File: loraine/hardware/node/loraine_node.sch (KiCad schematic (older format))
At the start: 41 parts, among them CON1 BARREL_JACK, IC1 ATTINY2313A-S, P1 POWER_THRU, P2 POWER, P3 SOLDER_PAD, P4 ICSP, P5 OUTPUTS, P6 BUS, P7 BUS_THRU, Q1 BD679, Q2 BD679, Q3 BD679, Q4 BD679, Q5 BD679, Q6 BD679, Q7 BD679, Q8 BD679, U1 UA7805CKCT, U2 SN65176BD, U3 TL4242, U4 TL4242, U5 TL4242, X1 16MHz

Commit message: Split boards
Removed LEDs and TL4242s and sense resistors from main node board and added 3x SIL3 connectors
Added 2nd board containing heatsunk LED mounting, TL4242, sense resistors.
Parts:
- removed D1: STAR_LED, symbol STAR_LED
- removed R1, R2, R3: R, symbol R
- removed U3, U4, U5: TL4242, symbol TL4242
- added K1, K2, K3: CONN_3, symbol CONN_3
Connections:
- net labels added: +5V
- wire segments 238 -> 154
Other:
- note removed: "3W star wants I=0.35A R=0.51\n1W star wants I=0.15A R=1.18"
- note removed: "Resistor dissipation is\n1W star: 60mW\n3W star: 27mW"
- note removed: "These current sense resistors\nset the peak LED current.\nREF is held at 177mV nominal\n"

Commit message: Proposed output driver for node h/w
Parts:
- removed Q1, Q2, Q3, Q4, Q5, Q6, Q7, Q8: BD679, symbol BD679
- added D?: DIODE, symbol DIODE
- added Q?: PNP, symbol PNP
- added Q?: MOS_N, symbol MOS_N
- added R? (x2): 10k, symbol R
- added R?: 560, symbol R
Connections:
- wire segments 154 -> 141
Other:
- note added: "ATtiny\nOutput"
- note added: "Load"

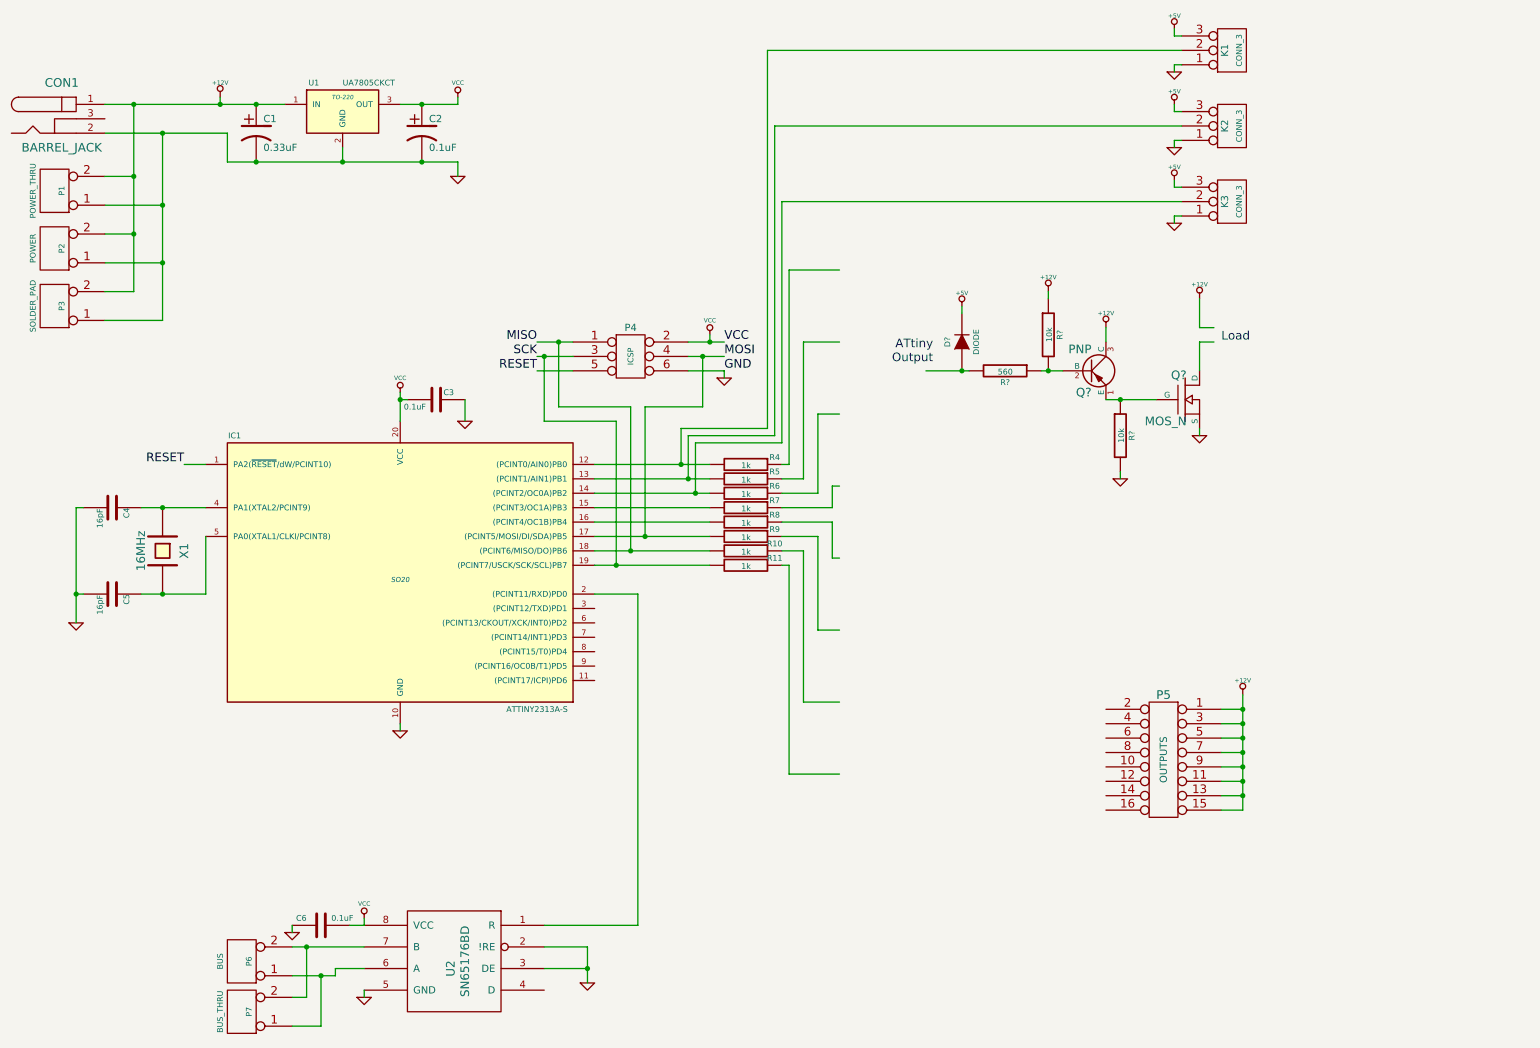
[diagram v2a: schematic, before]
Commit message: NMOS drivers on schematic + ERC fixes
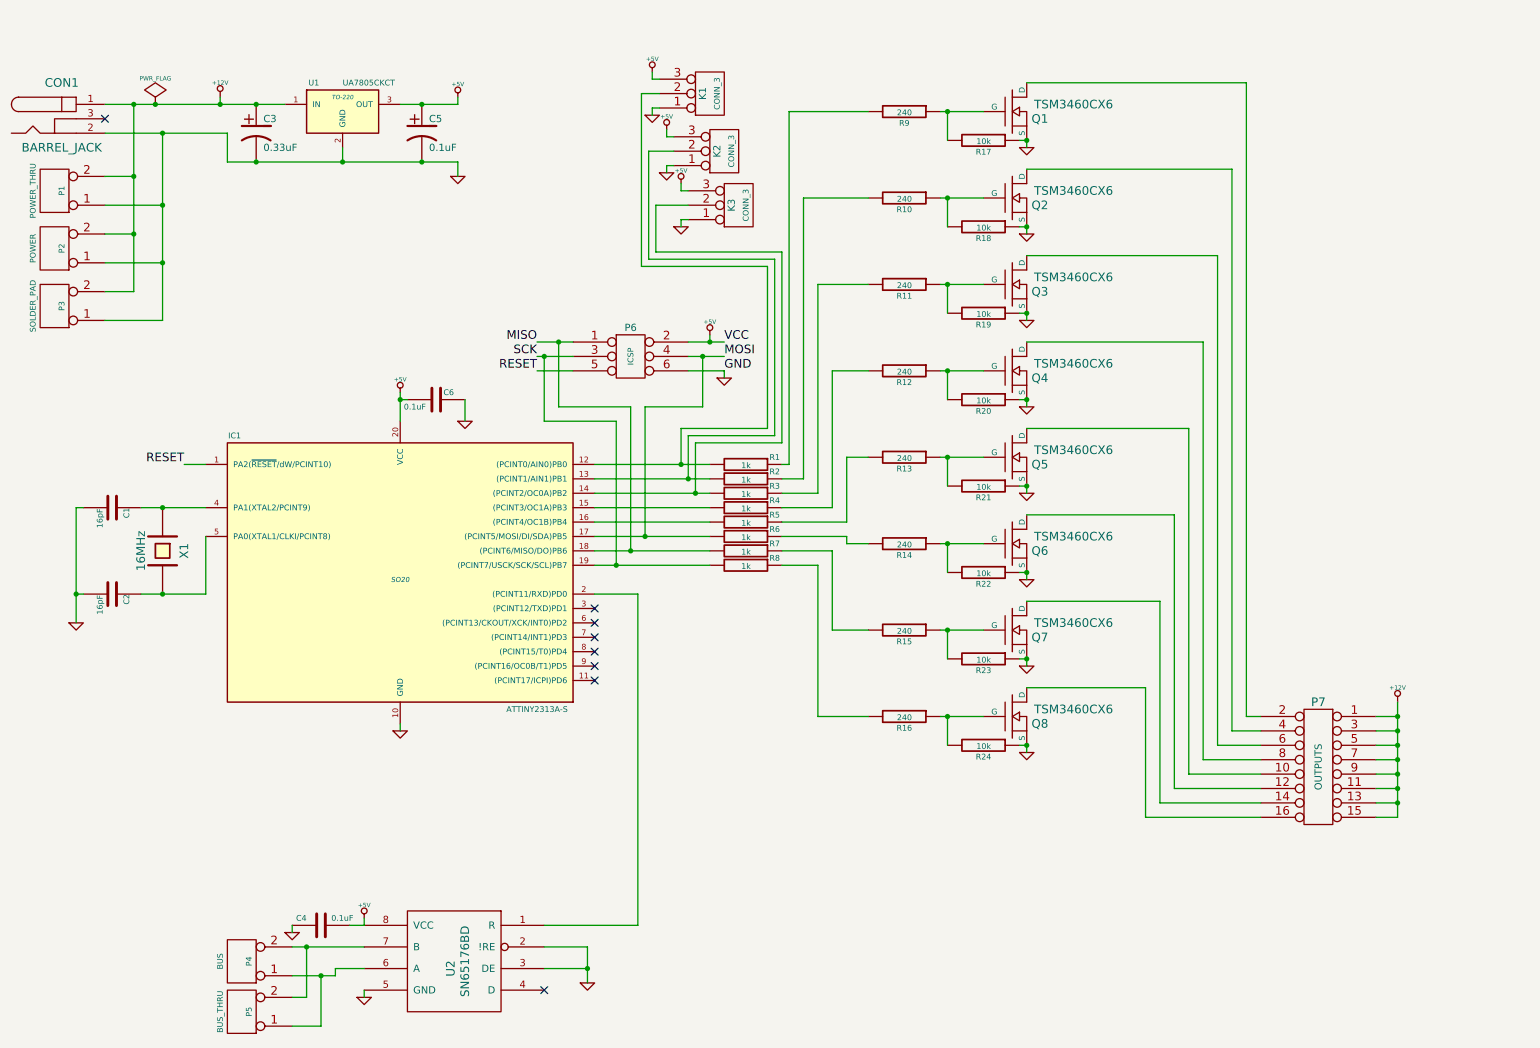
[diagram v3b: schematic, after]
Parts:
- removed D?: DIODE, symbol DIODE
- removed Q?: PNP, symbol PNP
- removed R?: 10k, symbol R
- added Q2, Q3, Q4, Q5, Q6, Q7, Q8: TSM3460CX6, symbol MOS_N
- added R10, R11, R12, R13, R14, R15, R16: 240, symbol R
- added R18, R19, R20, R21, R22, R23, R24: 10k, symbol R
- Q1: renamed from Q?; value MOS_N -> TSM3460CX6
- R9: renamed from R?; value 560 -> 240
- gave numbers to parts that had none: 1
- renumbered C4 to C1, C5 to C2, C1 to C3, C6 to C4, C2 to C5, C3 to C6, P6 to P4, P7 to P5, P4 to P6, P5 to P7, R4 to R1, R5 to R2, R6 to R3, R7 to R4, R8 to R5, R9 to R6, R10 to R7, R11 to R8
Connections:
- wire segments 141 -> 191
- no-connect marks 0 -> 8
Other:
- note removed: "ATtiny\nOutput"
- note removed: "Load"
- moved on the sheet: K1, K2, K3, P7, Q1, R17, R9

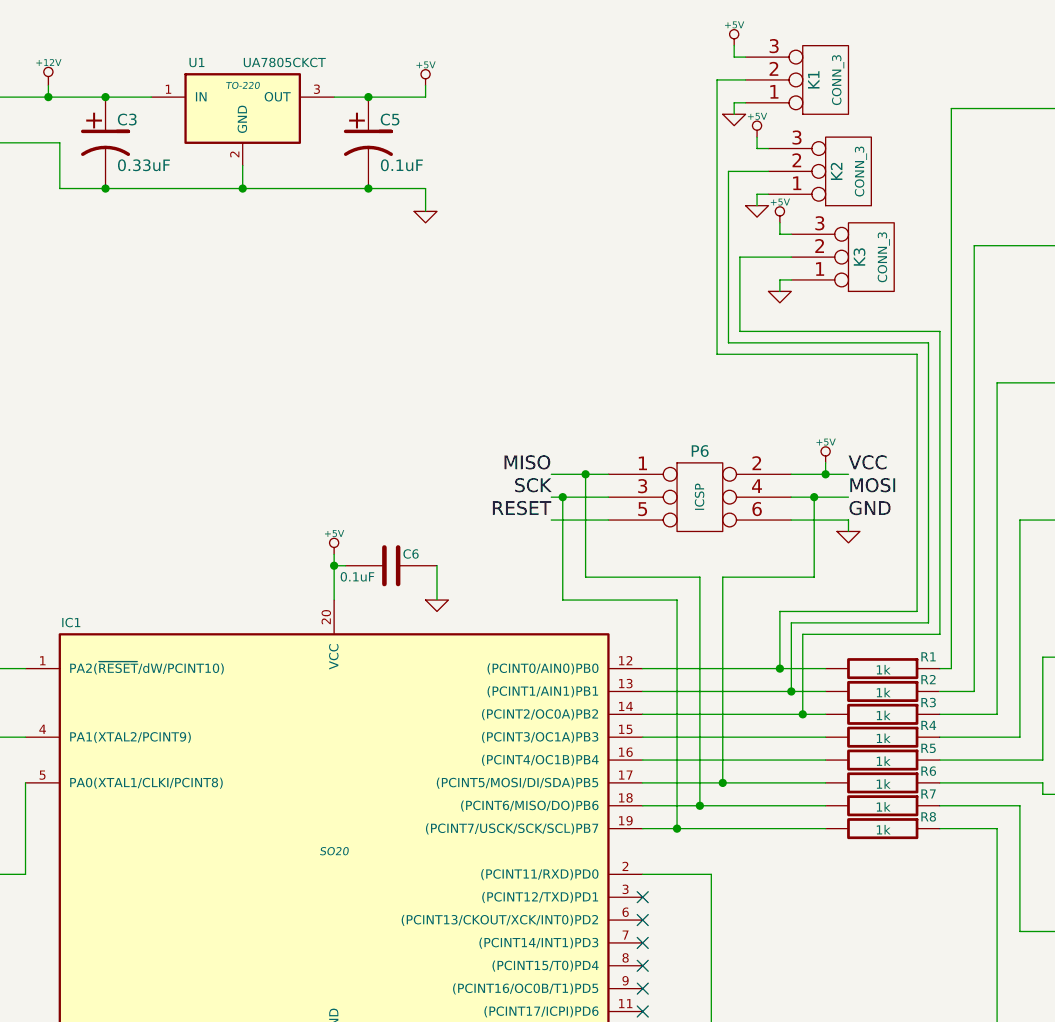
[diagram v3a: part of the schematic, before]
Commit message: Node PCB redo
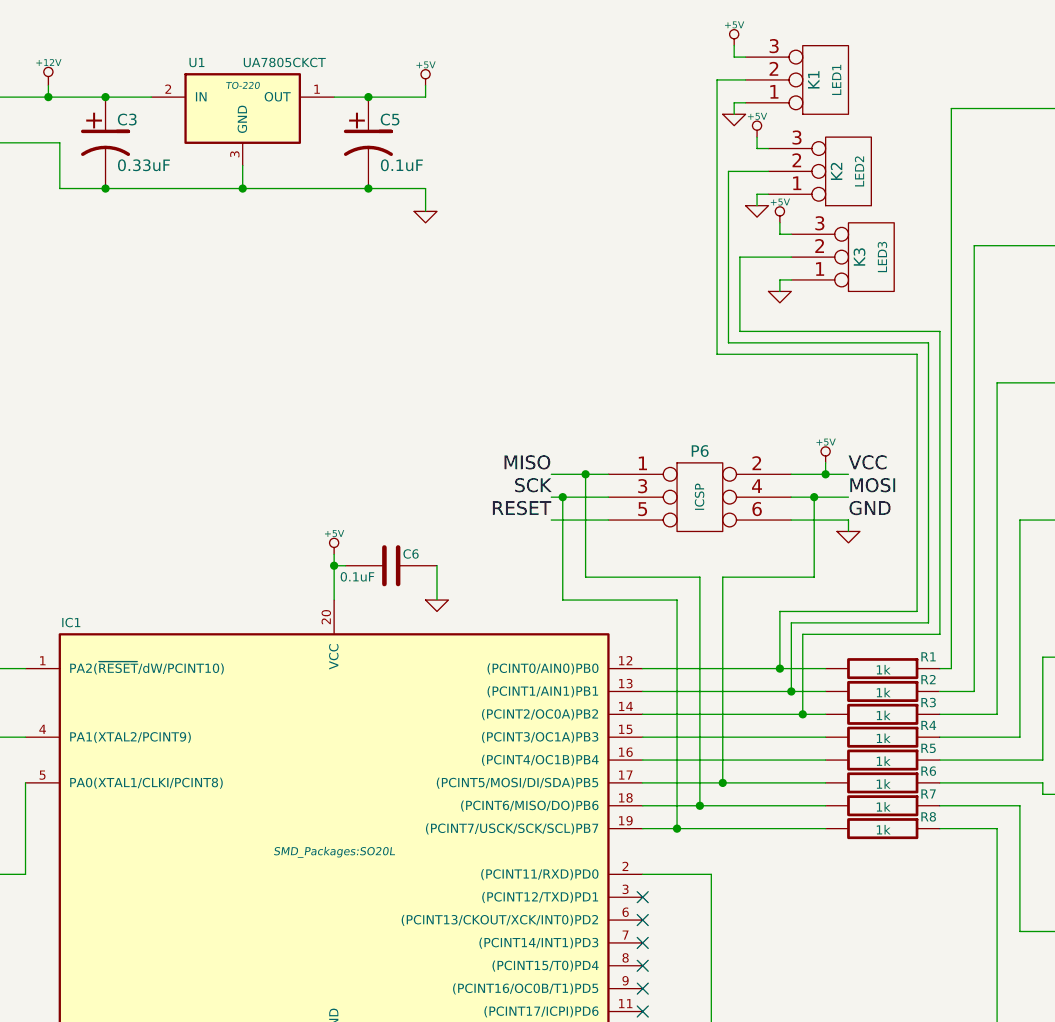
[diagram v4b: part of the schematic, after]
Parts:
- removed U1: UA7805CKCT, TO-220, symbol LM7805CT
- added U1: UA7805CKCT, TO-220, symbol UA7805CKCT
- C1, C2, C3, C4, C5, C6: footprint (none) -> Capacitors_SMD:c_0805
- CON1: footprint (none) -> Connect:BARREL_JACK
- IC1: footprint SO20 -> SMD_Packages:SO20L
- K1: value CONN_3 -> LED1; footprint (none) -> Connect:SIL-3
- K2: value CONN_3 -> LED2; footprint (none) -> Connect:SIL-3
- K3: value CONN_3 -> LED3; footprint (none) -> Connect:SIL-3
- P1, P2, P6, P7: footprint (none) -> molex-22-23-2021:SIL-2
- P3: footprint (none) -> solder_pad:SIL-2
- P4: footprint (none) -> Pin_Headers:Pin_Header_Straight_2x03
- P5: footprint (none) -> Pin_Headers:Pin_Header_Straight_2x08
- Q1, Q2, Q3, Q4, Q5, Q6, Q7, Q8: footprint (none) -> to126:TO126
- R1, R10, R11, R12, R13, R14, R15, R16, R17, R18, R19, R2, R20, R21, R22, R23, R24, R3, R4, R5, R6, R7, R8, R9: footprint (none) -> SMD_Packages:SM0805
- U2: footprint (none) -> SMD_Packages:SO8E
- X1: footprint (none) -> Crystals:Crystal_HC49-SD_SMD
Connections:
- net +12V: now also U1.2 (IN)
- net +5V: now also U1.1 (OUT)
- net GND: now also U1.3 (GND)
